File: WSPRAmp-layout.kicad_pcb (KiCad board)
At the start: 2 copper layers, 90 x 60 mm, 18 parts, among them J1 Conn_Coaxial_Small, J2 Conn_01x05, U3 T2N7002AK_G0_00

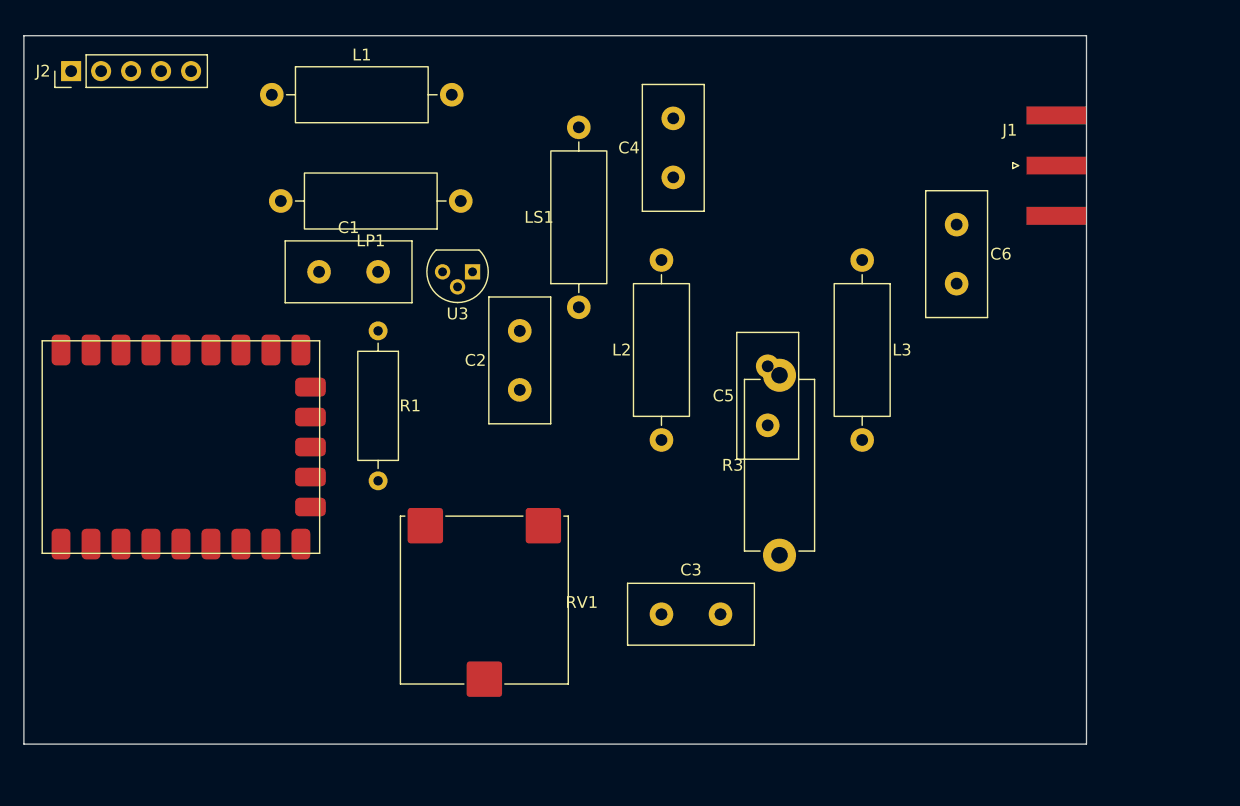
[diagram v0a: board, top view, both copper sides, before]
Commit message: Route WSPRAmp board and add upright FT37-43 assemblies
Reserve plug-in GPS space, pair transformer windings on one core, and add local footprints, 3D model, and schematic assignments. Verify zero DRC errors and unconnected items; retain known RP2040 footprint-library warning.
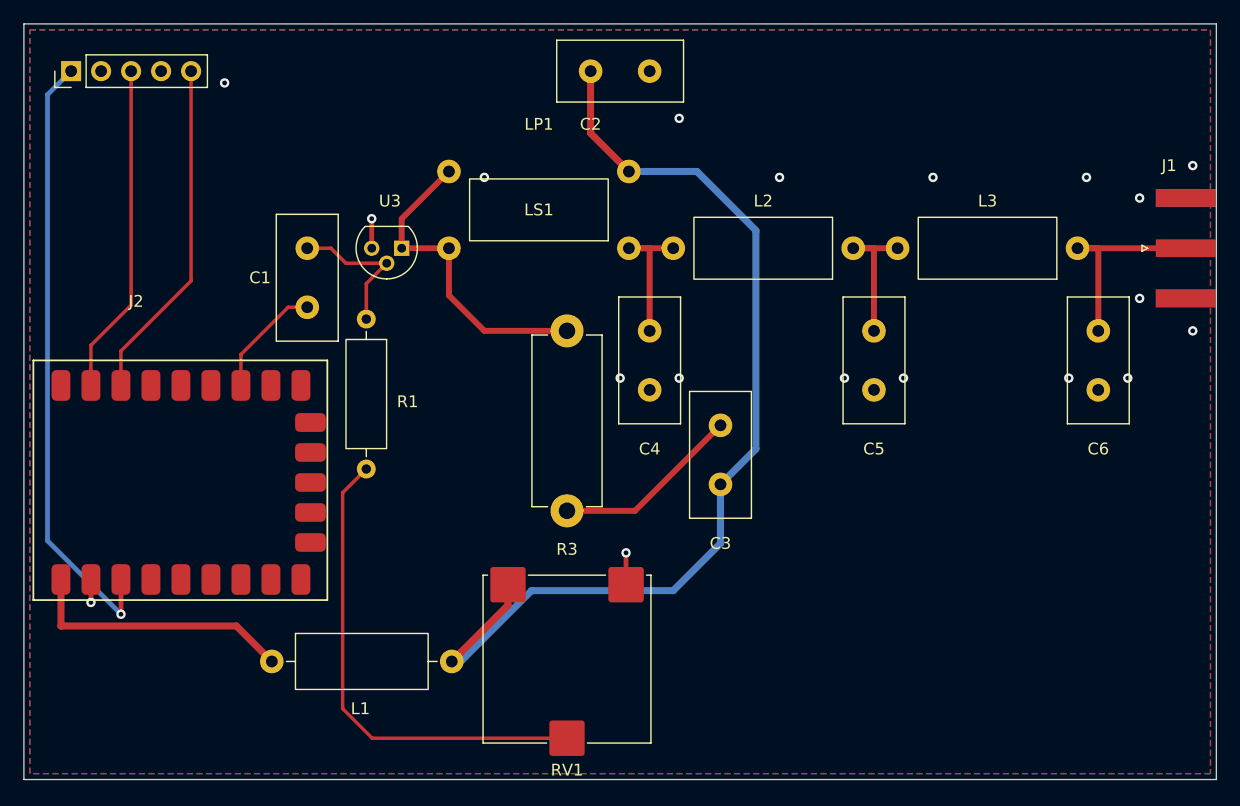
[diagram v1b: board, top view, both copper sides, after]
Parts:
- L2, L3: footprint Inductor_THT:L_Axial_L11.0mm_D4.5mm_P15.24mm_Horizontal_Fastron_MECC -> WSPRAmp:FT37-43_Upright_Inductor_P15.24mm
- LP1: footprint Inductor_THT:L_Axial_L11.0mm_D4.5mm_P15.24mm_Horizontal_Fastron_MECC -> WSPRAmp:FT37-43_Upright_Bifilar_Primary
- LS1: footprint Inductor_THT:L_Axial_L11.0mm_D4.5mm_P15.24mm_Horizontal_Fastron_MECC -> WSPRAmp:FT37-43_Upright_Bifilar_Secondary
- moved L1 48.0 mm to (61.0, 88.0)
- moved C2 27.7 mm to (88.0, 38.0), turned to 0 degrees
- moved L2 23.0 mm to (110.2, 53.0), turned to 180 degrees
- moved R3 18.4 mm to (86.0, 75.2)
- moved L3 18.3 mm to (129.2, 53.0), turned to 180 degrees
- moved C6 15.0 mm to (131.0, 60.0)
- moved LP1 14.5 mm to (91.2, 46.5)
- moved C4 13.2 mm to (93.0, 60.0), turned to -90 degrees
- moved J1 13.0 mm to (138.4, 53.0)
- moved C3 12.1 mm to (99.0, 73.0), turned to 90 degrees
- moved LS1 12.1 mm to (76.0, 53.0), turned to 0 degrees
- moved C5 12.0 mm to (112.0, 60.0), turned to -90 degrees
- moved RV1 8.60 mm to (86.0, 88.0)
- moved U3 6.32 mm to (72.0, 53.0)
- moved C1 3.16 mm to (64.0, 58.0), turned to 90 degrees
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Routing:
- net Net-(C2-Pad1): track 0.00 -> 85.8 mm
- net Net-(J2-Pin_1): track 0.00 -> 52.9 mm, vias 0 -> 1
- net Net-(R1-Pad2): track 0.00 -> 41.2 mm
- net Net-(J2-Pin_5): track 0.00 -> 29.7 mm
- net Net-(J2-Pin_3): track 0.00 -> 28.6 mm
- net Net-(U3-3): track 0.00 -> 27.4 mm
- net +5V: track 0.00 -> 23.6 mm
- net /out: track 0.00 -> 17.9 mm
- net Net-(C3-Pad2): track 0.00 -> 16.0 mm
- net Net-(U3-1): track 0.00 -> 12.7 mm
- net Net-(C5-Pad1): track 0.00 -> 12.5 mm
- net Net-(C4-Pad1): track 0.00 -> 12.5 mm
- net /PiGPIO4in: track 0.00 -> 10.5 mm
- net GND: track 0.00 -> 7.74 mm, vias 0 -> 19
- added copper zone on B.Cu, net GND
- added copper zone on F.Cu, net GND
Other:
- board size 90 x 60 mm -> 101 x 64 mm
